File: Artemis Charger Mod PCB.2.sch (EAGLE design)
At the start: 156 parts, among them J1 MOLEX_CLICKMATE-2-VERTICAL, J2 MOLEX_CLICKMATE-4-VERTICAL, J3 MOLEX_CLICKMATE-2-VERTICAL, J4 MOLEX_CLICKMATE-2-VERTICAL, J5 MOLEX_CLICKMATE-2-VERTICAL, J6 MOLEX_CLICKMATE-4-VERTICAL, Q10 BSS138, Q11 BSS138, Q8 BSS138, Q9 BSS138, U10 TPS562219, U11 ISO7340, U12 ISO7340, U13 TPS562219, U14 MCP2515-TSSOP, U15 MCP2562, U16 CD4050BD, U17 CD4050BD, U18 CD4043B, U19 SN74LVC08ASOIC, U20 SN74LVC32ASOIC, U22 LTC1155, U23 CSD17506Q5A, U24 LTC1155, U25 CD4050BD, U26 CSD17506Q5A, U27 LTC1155, U28 CSD17506Q5A, U29 LTC1155, U3 MAX5812, U30 CSD17506Q5A, U31 LTC1155, U32 CSD17506Q5A, U33 LTC1155, U34 CSD17506Q5A, U49 TL7712A-SOIC, U8 MAX5812, U9 TPS562219

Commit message: DONE
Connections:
- removed net +5V/1_CURRENT_SENSE: O1.VCC1
- net +3V3: now also O1.VCC1
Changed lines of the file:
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@@
 <instance part="SUPPLY7" gate="G$1" x="180.34" y="152.4"/>
 <instance part="SUPPLY20" gate="G$1" x="215.9" y="139.7"/>
-<instance part="SUPPLY21" gate="G$1" x="256.54" y="91.44" rot="R90"/>
+<instance part="SUPPLY21" gate="G$1" x="254" y="91.44" rot="R90"/>
 <instance part="SUPPLY23" gate="G$1" x="281.94" y="193.04" rot="R270"/>
 <instance part="P+2" gate="VCC" x="314.96" y="25.4"/>
@@
 </segment>
 </net>
-<net name="+5V/1_CURRENT_SENSE" class="0">
-<segment>
-<pinref part="O1" gate="G$1" pin="VCC1"/>
-<pinref part="SUPPLY21" gate="G$1" pin="+3V3"/>
-</segment>
-</net>
 <net name="N$4" class="0">
 <segment>
@@
 <pinref part="SUPPLY13" gate="G$1" pin="+3V3"/>
 <wire x1="332.74" y1="76.2" x2="335.28" y2="76.2" width="0.1524" layer="91"/>
+</segment>
+<segment>
+<pinref part="O1" gate="G$1" pin="VCC1"/>
+<pinref part="SUPPLY21" gate="G$1" pin="+3V3"/>
+<wire x1="256.54" y1="91.44" x2="259.08" y2="91.44" width="0.1524" layer="91"/>
 </segment>
 </net>
@@
 <wire x1="789.94" y1="358.14" x2="789.94" y2="320.04" width="0.1524" layer="91"/>
 <wire x1="789.94" y1="320.04" x2="744.22" y2="320.04" width="0.1524" layer="91"/>
-<wire x1="789.94" y1="320.04" x2="744.22" y2="320.04" width="0.1524" layer="91"/>
+<junction x="789.94" y="358.14"/>
 </segment>
 </net>
@@
 </sheet>
 </sheets>
+<errors>
+</errors>
 </schematic>
 </drawing>

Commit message: Added BOM
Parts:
- R1: PARTNO ERA-6AEB5492V -> 1676307-2
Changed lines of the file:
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@@
 </part>
 <part name="R1" library="adafruit" deviceset="R-US_" device="R0805" value="33.2k">
-<attribute name="PARTNO" value="ERA-6AEB5492V"/>
+<attribute name="PARTNO" value="1676307-2"/>
 </part>
 <part name="C2" library="adafruit" deviceset="C-US" device="C0805" value="10uF">

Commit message: Fixed list of errors: Too many vias around regulators
Make +5V plane in cover all area in isolated region

Make isolation barrier a simple rectangle

rotate +5v regulator (isolated area) 180deg so that the current path is more direct

More vias/planes at connectors

Give nets a descriptive name

Use vector font

U16/17/25 should combine into one part

bypass caps on ICs

U22/24/27/29/31/33 can be combined into 3 parts

RTDS_SOURCE is connected to FETs that it shouldn't be

U18 has a floating EN pin

use planes for current paths to the FETs, and make sure to connect to all of the pads (3 source, 4+pad drain)

Check pin current limits of connectors

Can use 10mil traces if needed for signals

Add mark to indicate pin 1 of RasPi connector

Watch mechanical clearances at the end of ICs, there are some that are really close

Q10/11 level shifters have pull downs. Does this work?

Label the connectors on the PCB so we know what they connect to.

Do we really need testpoints on every FET driver input/output?

Supply layer planes are a mess

Check RasPi power pins. There are multiple 5v and GND. Currently use 1 5V and no GND

RasPi Pin 6 is connected to the ground of one of the isolators, but not to the GND1 net

RasPi SPI interface is wired wrong

RasPi pin 39 is connected to the board as an I/O, but it is a GND pin
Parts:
- removed R40, R42, R44: 10k, rcl:R-US_R0805
- removed U16, U25: CD4050BD, FormE:CD4050BD
- removed U24, U31, U33: LTC1155, FormE:LTC1155
- added C35, C36: 1uF, rcl:C-USC0805
- O1: PARTNO (none) -> ISO1541DR
- S1: PARTNO (none) -> FSM4JSMATR
- U11, U12: PARTNO (none) -> ISO7340CDWR
- U3, U8: PARTNO (none) -> MAX5812LEUT+T
- Y1: PARTNO (none) -> ECS-160-20-3X-TR
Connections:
- net MO renamed SO_SPI
- net N$10 renamed SCL1_I2C
- net N$1000 renamed SCL
- net N$11 renamed ADD
- net N$24 renamed ADJ_EMULATOR_IN_2
- net N$27 renamed ADJ_EMULATOR_IN_4
- net N$29 renamed ADJ_EMULATOR_IN_3
- net N$34 renamed LED_TO_PI_4
- net N$35 renamed LED_TO_PI_3
- net N$36 renamed LED_TO_PI_2
- net N$37 renamed LED_TO_PI_1
- net N$5 renamed ADJ_EMULATOR_IN_1
- net N$7 renamed SDA
- net N$70 renamed CS_SPI
- net RTDS_SOURCE2 renamed ACUMULATOR_CONTACTOR_SIGNAL
- net SCK renamed SCK_SPI
- removed net N$18: JP1.6, O1.GND1
- removed net N$48: H4.6, U15.STBY
- new net FET_CONNECT_1: TP30.TP, U23.S, U26.D
- new net FET_CONNECT_2: TP1.TP, U26.S, U28.D
- new net SDA1_I2C: JP1.3, O1.SDA1, R34.2
- net +3V3: now also C35.1, C36.1, U14.VDD, U15.SPLIT/VIO, U18EN.EN, U18P.VCC, U19P.VCC, U20P.VCC, U21POWER.VCC
- net +5V/1: now also JP1.4; no longer U14.VDD, U15.SPLIT/VIO
- net AMS_15V_FILTERED: now also U17B.OUT; no longer R42.1, U25D.OUT
- net AMS_BACK_TO_PI: now also JP1.37; no longer JP1.39
- net BSPD_FET_SIGNAL: now also U22B.IN; no longer U24A.IN
- net BSPD_FET_SIGNAL1: now also U27B.IN; no longer U31A.IN
- net BSPD_FET_SIGNAL3: now also U29B.IN; no longer U33A.IN
- net GND1: now also C35.2, C36.2, JP1.14, JP1.20, JP1.25, JP1.30, JP1.34, JP1.6, JP1.9, O1.GND1, U15.STBY; no longer R42.2, R44.2, U16POWER.GND, U24P.GND, U25POWER.GND, U31P.GND, U33P.GND
- net IMD_15V_FILTERED: now also U17A.OUT; no longer R40.1, U17D.OUT
- net INTERUPT_LINES_15V_FILTERED: now also U17C.OUT; no longer R44.1, U16D.OUT
- net INTERUPT_LINES_BACK_TO_PI: now also JP1.35; no longer JP1.37
- net N$43: now also U17B.IN; no longer U25D.IN
- net N$50: now also U17C.IN; no longer U16D.IN
- net N$53: now also U17A.IN; no longer U17D.IN
- net N$55: now also U22B.G; no longer U24A.G
- net N$59: now also U27B.G; no longer U31A.G
- net N$64: now also U29B.G; no longer U33A.G
- net N$9: no longer JP1.3, O1.SDA1, R34.2
- net RTDS_SOURCE: no longer TP1.TP, TP30.TP, U23.S, U26.D, U26.S, U28.D
- net VDD: now also U22B.D, U27B.D, U29B.D; no longer R40.2, U16POWER.VCC, U18P.VCC, U19P.VCC, U20P.VCC, U21POWER.VCC, U24A.D, U24P.VCC, U25POWER.VCC, U31A.D, U31P.VCC, U33A.D, U33P.VCC
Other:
- note removed: "Also U17"
- note removed: "Connected to 5v/1 current sense not 5V/1 ??????"
- note removed: "Mosfets want to go to GND not GND1 But invoke doesnt work?!?!?!?!?!?!?!?!?"
- note removed: "U18 is tied to something on charger side ???????????"
- note removed: "Why Nets Connected?????"

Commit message: Started cleaning up layout
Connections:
- new net N$3: H4.3
- net GND1: now also JP1.39
- net N$25: now also H2.7; no longer H2.8
- net N$26: now also H2.8; no longer H2.7
- net N$42: no longer H4.3
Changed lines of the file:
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@@
 <?xml version="1.0" encoding="utf-8"?>
 <!DOCTYPE eagle SYSTEM "eagle.dtd">
-<eagle version="7.5.0">
+<eagle version="7.3.0">
 <drawing>
 <settings>
@@
 <attribute name="PARTNO" value="EMK212B7105KG-T"/>
 </part>
+<part name="SUPPLY61" library="supply2" deviceset="GND1" device=""/>
 </parts>
 <sheets>
@@
 <attribute name="PARTNO" x="543.56" y="208.28" size="1.778" layer="96" display="off"/>
 </instance>
+<instance part="SUPPLY61" gate="G$1" x="254" y="144.78" rot="R270"/>
 </instances>
 <busses>
@@
 <pinref part="C35" gate="G$1" pin="2"/>
 </segment>
+<segment>
+<pinref part="SUPPLY61" gate="G$1" pin="GND1"/>
+<pinref part="JP1" gate="A" pin="39"/>
+<wire x1="256.54" y1="144.78" x2="266.7" y2="144.78" width="0.1524" layer="91"/>
+</segment>
 </net>
 <net name="N$19" class="0">
@@
 <segment>
 <pinref part="U3" gate="G$1" pin="OUT"/>
-<wire x1="279.4" y1="20.32" x2="297.18" y2="20.32" width="0.1524" layer="91"/>
-<pinref part="H2" gate="G$1" pin="8"/>
-<wire x1="297.18" y1="20.32" x2="297.18" y2="15.24" width="0.1524" layer="91"/>
+<wire x1="279.4" y1="20.32" x2="299.72" y2="20.32" width="0.1524" layer="91"/>
+<pinref part="H2" gate="G$1" pin="7"/>
+<wire x1="299.72" y1="20.32" x2="299.72" y2="15.24" width="0.1524" layer="91"/>
 </segment>
 </net>
@@
 <segment>
 <pinref part="U8" gate="G$1" pin="OUT"/>
-<pinref part="H2" gate="G$1" pin="7"/>
-<wire x1="279.4" y1="48.26" x2="299.72" y2="48.26" width="0.1524" layer="91"/>
-<wire x1="299.72" y1="48.26" x2="299.72" y2="15.24" width="0.1524" layer="91"/>
+<wire x1="279.4" y1="48.26" x2="297.18" y2="48.26" width="0.1524" layer="91"/>
+<pinref part="H2" gate="G$1" pin="8"/>
+<wire x1="297.18" y1="48.26" x2="297.18" y2="15.24" width="0.1524" layer="91"/>
 </segment>
 </net>
@@
 <wire x1="325.12" y1="55.88" x2="335.28" y2="55.88" width="0.1524" layer="91"/>
 <wire x1="302.26" y1="63.5" x2="325.12" y2="63.5" width="0.1524" layer="91"/>
+<label x="231.14" y="177.8" size="1.778" layer="95"/>
 </segment>
 </net>
@@
 <wire x1="327.66" y1="60.96" x2="335.28" y2="60.96" width="0.1524" layer="91"/>
 <wire x1="304.8" y1="66.04" x2="327.66" y2="66.04" width="0.1524" layer="91"/>
+<label x="231.14" y="175.26" size="1.778" layer="95"/>
 </segment>
 </net>
@@
 <pinref part="H4" gate="G$1" pin="7"/>
 <wire x1="444.5" y1="243.84" x2="444.5" y2="259.08" width="0.1524" layer="91"/>
+<label x="444.5" y="254" size="1.778" layer="95" rot="R270"/>
 </segment>
 </net>
@@
 <wire x1="452.12" y1="259.08" x2="452.12" y2="251.46" width="0.1524" layer="91"/>
 <junction x="452.12" y="251.46"/>
+<label x="233.68" y="180.34" size="1.778" layer="95"/>
 </segment>
 </net>
 <net name="N$42" class="0">
 <segment>
-<pinref part="H4" gate="G$1" pin="3"/>
-<wire x1="434.34" y1="259.08" x2="434.34" y2="254" width="0.1524" layer="91"/>
-<wire x1="434.34" y1="254" x2="436.88" y2="254" width="0.1524" layer="91"/>
 <pinref part="H4" gate="G$1" pin="4"/>
 <wire x1="436.88" y1="254" x2="436.88" y2="259.08" width="0.1524" layer="91"/>
@@
 <wire x1="914.4" y1="411.48" x2="914.4" y2="233.68" width="0.1524" layer="91"/>
 <wire x1="914.4" y1="233.68" x2="439.42" y2="233.68" width="0.1524" layer="91"/>
+<label x="439.42" y="254" size="1.778" layer="95" rot="R270"/>
 </segment>
 </net>
@@
 </segment>
 </net>
+<net name="N$3" class="0">
+<segment>
+<pinref part="H4" gate="G$1" pin="3"/>
+<wire x1="434.34" y1="259.08" x2="434.34" y2="254" width="0.1524" layer="91"/>
+</segment>
+</net>

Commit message: Fixed second list of errors:  Decoupling capacitors
U11/12 EN pin is floating

Don't use solid planes at FET drivers

Lots of random vias

Planes from FETs to contactor connector

Connector labels

Cleanup supply layer planes

Isolation line needs to be thru center of isolators

unnecessary vias at raspi connector

SPI interface
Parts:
- removed J6: MOLEX_CLICKMATE-4-VERTICAL, FormE:MOLEX_CLICKMATE-4-VERTICAL
- removed R14: 10K, adafruit:R-US_R0805
- added C33, C34, C37, C38, C41, C42, C43, C44, C45, C46: 0.1uF, rcl:C-USC0805
- added R38: 10K, adafruit:R-US_R0805
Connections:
- net ADJ_EMULATOR_IN_1 renamed TIMER_ADJ_1
- net ADJ_EMULATOR_IN_2 renamed TIMER_ADJ_2
- net ADJ_EMULATOR_IN_3 renamed TIMER_ADJ_3
- net ADJ_EMULATOR_IN_4 renamed TIMER_ADJ_4
- removed net CAN_HIGH: H4.7, R17.1, U15.CANH
- removed net MI: JP1.26, TP12.TP, U14.SI
- removed net N$38: JP1.18, U12.OUTA
- removed net N$39: JP1.16, U12.OUTB
- removed net N$40: JP1.12, U12.OUTC
- removed net N$41: JP1.7, U12.OUTD
- removed net N$42: H4.4
- removed net N$51: H4.8, R17.2, U15.CANL
- removed net N$52: H4.10, JP1.11, R14.1
- new net CAN_N: H4.5, R17.2, U15.CANL
- new net CAN_P: H4.4, R17.1, U15.CANH
- new net LED_TO_PI_1_C: H3.1, U12.IND
- new net LED_TO_PI_2_C: H3.2, U12.INC
- new net LED_TO_PI_3_C: H3.3, U12.INB
- new net LED_TO_PI_4_C: H3.4, U12.INA
- new net SI_SPI: JP1.19, TP15.TP, U14.SI
- net +3V3: now also C37.1, C38.1, C41.1, C42.1
- net +5V: now also C33.1, C34.1
- net ACUMULATOR_CONTACTOR_SIGNAL: now also H4.3; no longer H4.5
- net AMS15V: now also H4.6; no longer J6.2
- net CS_SPI: now also JP1.24, TP4.TP; no longer JP1.21, TP19.TP
- net GND: now also C33.2, C34.2
- net GND1: now also C37.2, C38.2, C41.2, C42.2, C43.2, C44.2, C45.2, C46.2, H4.10, R38.1; no longer R14.2
- net IMD15V: now also H4.7; no longer J6.3
- net INTERUPT15V: now also H4.8; no longer J6.1
- net LED_TO_PI_1: now also JP1.18, U12.OUTA; no longer H3.1, U12.IND
- net LED_TO_PI_2: now also JP1.16, U12.OUTB; no longer H3.2, U12.INC
- net LED_TO_PI_3: now also JP1.12, U12.OUTC; no longer H3.3, U12.INB
- net LED_TO_PI_4: now also JP1.7, U12.OUTD; no longer H3.4, U12.INA
- net N$3: now also JP1.11, R38.2; no longer H4.3
- net N$49: no longer JP1.38
- net N$68: no longer JP1.36
- net SCK_SPI: now also JP1.23, TP19.TP; no longer JP1.24, TP4.TP
- net SCL1_I2C: now also JP1.3; no longer JP1.5
- net SDA1_I2C: now also JP1.5; no longer JP1.3
- net SO_SPI: now also JP1.21, TP12.TP; no longer JP1.23, TP15.TP
- net VDD: now also C43.1, C44.1, C45.1, C46.1
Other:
- note added: "CAN <---> SPI"
- note removed: "<- Both to IO Pannle ->"
- note removed: "To GIO on PI"
- note removed: "down to grd for AMS and interupt lines"
- moved on the sheet: C27, C35, H4, R34, R35, TP12, TP15, TP19, TP4

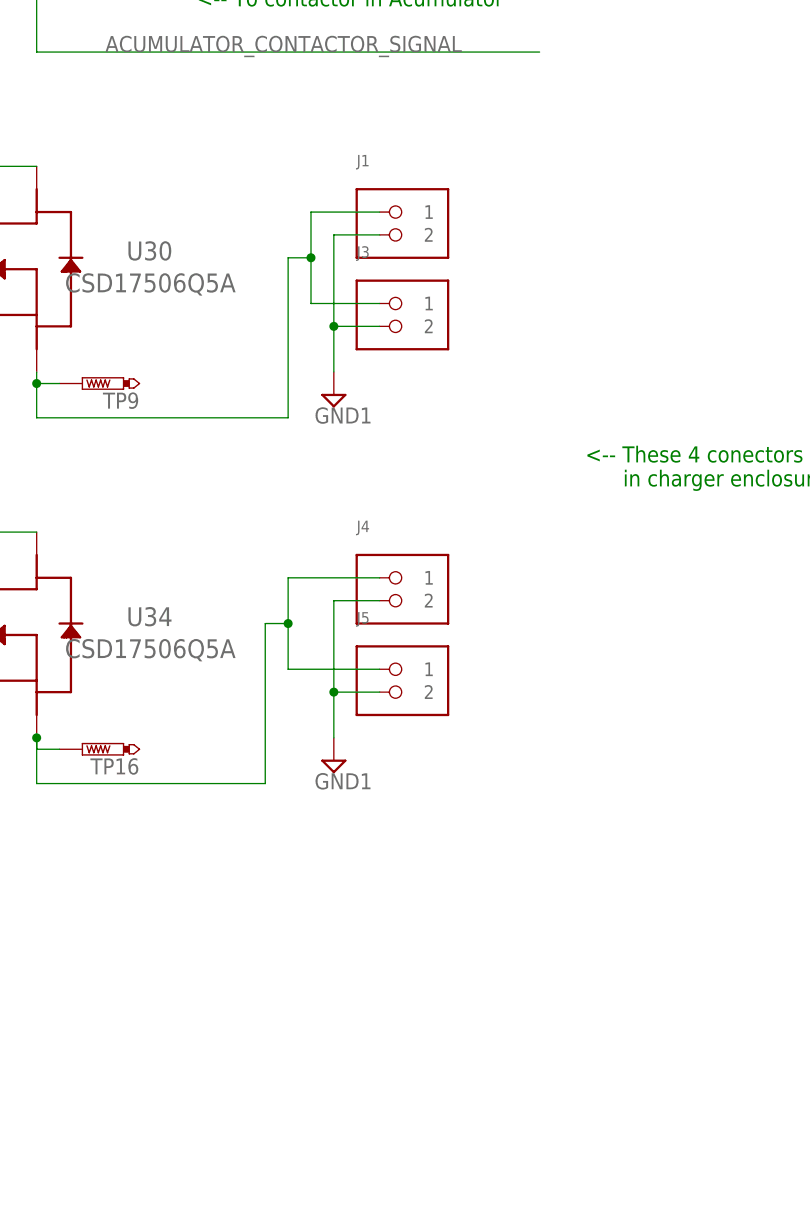
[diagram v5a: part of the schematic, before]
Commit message: Added extra contactor for charger discharge
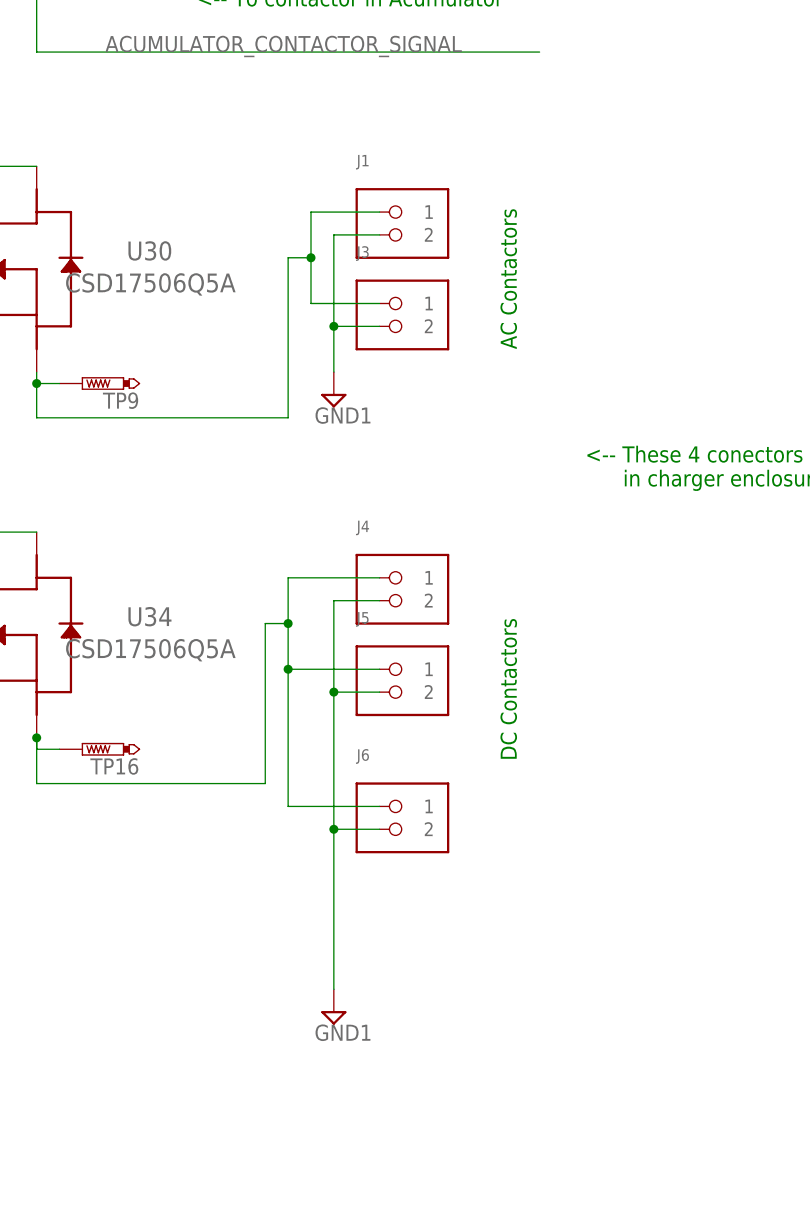
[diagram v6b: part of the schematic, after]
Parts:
- added J6: MOLEX_CLICKMATE-2-VERTICAL, FormE:MOLEX_CLICKMATE-2-VERTICAL
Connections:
- net GND1: now also J6.2
- net N$6: now also J6.1
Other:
- note added: "AC Contactors"
- note added: "DC Contactors"
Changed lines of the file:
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@@
 </part>
 <part name="SUPPLY58" library="supply1" deviceset="+3V3" device=""/>
+<part name="J6" library="FormE" deviceset="MOLEX_CLICKMATE-2-VERTICAL" device=""/>
 </parts>
 <sheets>
@@
 <text x="876.3" y="416.56" size="1.778" layer="91">&lt;-- To contactor in Acumulator</text>
 <text x="500.38" y="241.3" size="6.4516" layer="95">CAN &lt;---&gt; SPI</text>
+<text x="911.86" y="332.74" size="1.778" layer="91" rot="R90">DC Contactors</text>
+<text x="911.86" y="378.46" size="1.778" layer="91" rot="R90">AC Contactors</text>
 </plain>
 <instances>
@@
 <instance part="J5" gate="G$1" x="904.24" y="340.36"/>
 <instance part="SUPPLY16" gate="G$1" x="891.54" y="373.38"/>
-<instance part="SUPPLY17" gate="G$1" x="891.54" y="332.74"/>
+<instance part="SUPPLY17" gate="G$1" x="891.54" y="304.8"/>
 <instance part="SUPPLY18" gate="G$1" x="695.96" y="370.84" rot="R180"/>
 <instance part="SUPPLY19" gate="G$1" x="695.96" y="403.86" rot="R180"/>
@@
 </instance>
 <instance part="SUPPLY58" gate="G$1" x="546.1" y="177.8"/>
+<instance part="J6" gate="G$1" x="904.24" y="325.12"/>
 </instances>
 <busses>
@@
 <wire x1="891.54" y1="340.36" x2="896.62" y2="340.36" width="0.1524" layer="91"/>
 <junction x="891.54" y="340.36"/>
-<wire x1="891.54" y1="340.36" x2="891.54" y2="335.28" width="0.1524" layer="91"/>
+<wire x1="891.54" y1="340.36" x2="891.54" y2="325.12" width="0.1524" layer="91"/>
+<pinref part="J6" gate="G$1" pin="2"/>
+<wire x1="891.54" y1="325.12" x2="891.54" y2="307.34" width="0.1524" layer="91"/>
+<wire x1="891.54" y1="325.12" x2="896.62" y2="325.12" width="0.1524" layer="91"/>
+<junction x="891.54" y="325.12"/>
 </segment>
 <segment>
@@
 <wire x1="883.92" y1="347.98" x2="886.46" y2="347.98" width="0.1524" layer="91"/>
 <junction x="886.46" y="347.98"/>
-</segment>
-</net>
+<wire x1="886.46" y1="342.9" x2="886.46" y2="327.66" width="0.1524" layer="91"/>
+<junction x="886.46" y="342.9"/>
+<pinref part="J6" gate="G$1" pin="1"/>
+<wire x1="886.46" y1="327.66" x2="896.62" y2="327.66" width="0.1524" layer="91"/>
+</segment>
+</net>

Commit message: Fixed fixed silk screens, fixed a few overlap errors
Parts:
- removed R38: 10K, adafruit:R-US_R0805
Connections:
- removed net N$3: JP1.11, R38.2
- net GND1: no longer R38.1
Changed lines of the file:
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@@
 </part>
 <part name="SUPPLY54" library="supply2" deviceset="GND1" device=""/>
-<part name="R38" library="adafruit" deviceset="R-US_" device="R0805" value="10K">
-<attribute name="PARTNO" value="ERJ-6ENF1002V"/>
-</part>
 <part name="C33" library="rcl" deviceset="C-US" device="C0805" value="0.1uF">
 <attribute name="MF" value=""/>
@@
 </instance>
 <instance part="SUPPLY54" gate="G$1" x="279.4" y="119.38"/>
-<instance part="R38" gate="G$1" x="228.6" y="180.34">
-<attribute name="PARTNO" x="228.6" y="180.34" size="1.778" layer="96" rot="R270" display="off"/>
-</instance>
 <instance part="C33" gate="G$1" x="243.84" y="43.18" smashed="yes">
 <attribute name="NAME" x="244.856" y="43.815" size="1.778" layer="95"/>
@@
 <pinref part="JP1" gate="A" pin="25"/>
 <wire x1="266.7" y1="162.56" x2="261.62" y2="162.56" width="0.1524" layer="91"/>
-<pinref part="R38" gate="G$1" pin="1"/>
-<wire x1="223.52" y1="180.34" x2="223.52" y2="134.62" width="0.1524" layer="91"/>
-<wire x1="223.52" y1="134.62" x2="261.62" y2="134.62" width="0.1524" layer="91"/>
-<junction x="261.62" y="134.62"/>
 </segment>
 <segment>
@@
 <wire x1="370.84" y1="254" x2="406.4" y2="254" width="0.1524" layer="91"/>
 <label x="388.62" y="254" size="1.778" layer="95"/>
-<wire x1="406.4" y1="254" x2="406.4" y2="302.26" width="0.1524" layer="91"/>
-<wire x1="406.4" y1="302.26" x2="365.76" y2="302.26" width="0.1524" layer="91"/>
-<wire x1="365.76" y1="302.26" x2="365.76" y2="347.98" width="0.1524" layer="91"/>
+<pinref part="H4" gate="G$1" pin="8"/>
+</segment>
+<segment>
 <pinref part="R19" gate="G$1" pin="2"/>
 <wire x1="383.54" y1="345.44" x2="396.24" y2="345.44" width="0.1524" layer="91"/>
@@
 <wire x1="383.54" y1="342.9" x2="383.54" y2="345.44" width="0.1524" layer="91"/>
 <junction x="383.54" y="345.44"/>
-<wire x1="378.46" y1="345.44" x2="383.54" y2="345.44" width="0.1524" layer="91"/>
+<wire x1="365.76" y1="345.44" x2="383.54" y2="345.44" width="0.1524" layer="91"/>
 <label x="378.46" y="345.44" size="1.778" layer="95"/>
-<wire x1="365.76" y1="347.98" x2="378.46" y2="347.98" width="0.1524" layer="91"/>
-<wire x1="378.46" y1="347.98" x2="378.46" y2="345.44" width="0.1524" layer="91"/>
-<pinref part="H4" gate="G$1" pin="8"/>
 </segment>
 </net>
@@
 </segment>
 </net>
-<net name="N$3" class="0">
-<segment>
-<pinref part="JP1" gate="A" pin="11"/>
-<wire x1="233.68" y1="180.34" x2="266.7" y2="180.34" width="0.1524" layer="91"/>
-<pinref part="R38" gate="G$1" pin="2"/>
-</segment>
-</net>

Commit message: Added molex 1 pin and 2X20 header to BOM
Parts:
- C9: PARTNO GRM21BR71E104KA01L -> 5025841170
- JP1: PARTNO (none) -> 68602-220HLF
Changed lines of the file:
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@@
 <attribute name="PARTNO" value="MAX5812LEUT+T"/>
 </part>
-<part name="JP1" library="pinhead" deviceset="PINHD-2X20" device=""/>
+<part name="JP1" library="pinhead" deviceset="PINHD-2X20" device="">
+<attribute name="PARTNO" value="68602-220HLF"/>
+</part>
 <part name="P+1" library="supply1" deviceset="+5V" device=""/>
 <part name="LED3" library="FormE" deviceset="LED" device="CHIPLED_0805" value="GREEN">
@@
 <part name="P+4" library="supply1" deviceset="+5V" device=""/>
 <part name="C9" library="adafruit" deviceset="C-US" device="C0805" value="0.1uF">
-<attribute name="PARTNO" value="GRM21BR71E104KA01L"/>
+<attribute name="PARTNO" value="5025841170"/>
 </part>
 <part name="R7" library="adafruit" deviceset="R-US_" device="R0805" value="54.9k">
@@
 <attribute name="PARTNO" x="269.24" y="15.24" size="1.778" layer="96" display="off"/>
 </instance>
-<instance part="JP1" gate="A" x="269.24" y="170.18"/>
+<instance part="JP1" gate="A" x="269.24" y="170.18">
+<attribute name="PARTNO" x="269.24" y="170.18" size="1.778" layer="96" display="off"/>
+</instance>
 <instance part="P+1" gate="1" x="180.34" y="73.66"/>
 <instance part="LED3" gate="G$1" x="215.9" y="53.34">
